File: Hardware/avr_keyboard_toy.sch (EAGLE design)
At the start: 20 parts, among them IC1 7805T, IC2 MCP23017SP, U1 ATMEGA328P-PU

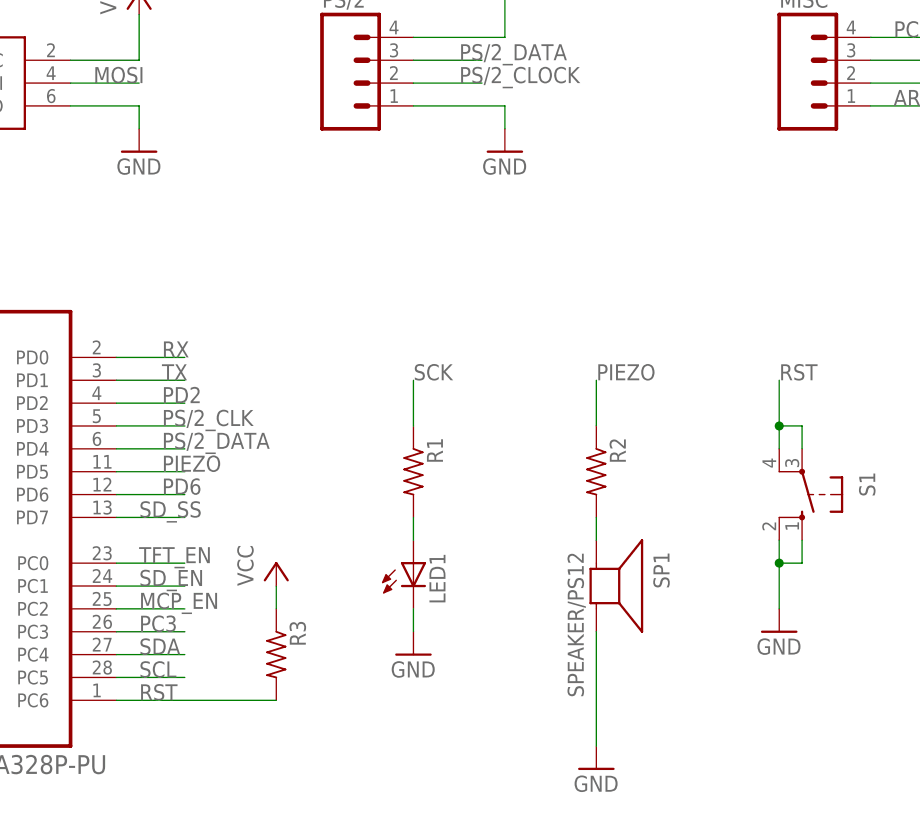
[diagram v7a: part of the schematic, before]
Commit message: Finished layout for rev. A board
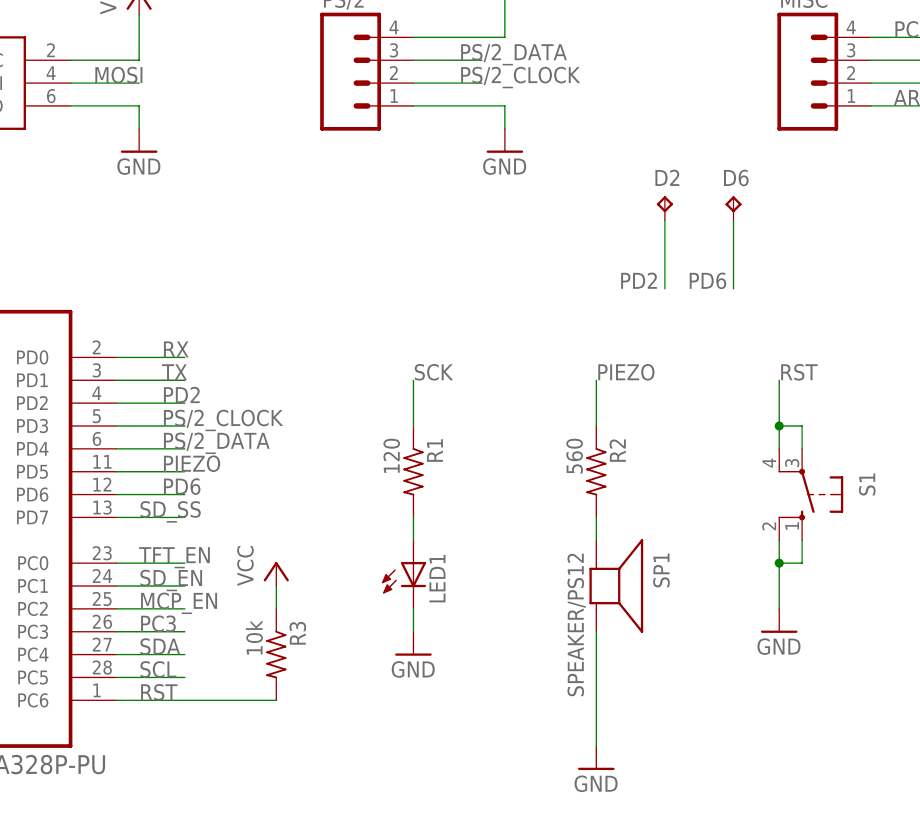
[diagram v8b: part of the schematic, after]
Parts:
- added D2, D6: TPB1,27, testpad:TPB1,27
- R1: value (none) -> 120
- R2: value (none) -> 560
- R3: value (none) -> 10k
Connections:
- removed net PS/2_CLK: U1.PD3
- net PD2: now also D2.TP
- net PD6: now also D6.TP
- net PS/2_CLOCK: now also U1.PD3
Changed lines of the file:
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@@
 <part name="ISP1" library="adafruit" deviceset="AVRISP" device="-6"/>
 <part name="LED1" library="adafruit" deviceset="LED" device="3MM"/>
-<part name="R1" library="adafruit" deviceset="R-US_" device="0204/5"/>
-<part name="R2" library="adafruit" deviceset="R-US_" device="0204/5"/>
-<part name="R3" library="adafruit" deviceset="R-US_" device="0204/5"/>
+<part name="R1" library="adafruit" deviceset="R-US_" device="0204/5" value="120"/>
+<part name="R2" library="adafruit" deviceset="R-US_" device="0204/5" value="560"/>
+<part name="R3" library="adafruit" deviceset="R-US_" device="0204/5" value="10k"/>
 <part name="SP1" library="adafruit" deviceset="SPEAKER" device="/PS12"/>
 <part name="S1" library="switch-omron" deviceset="10-XX" device=""/>
@@
 <part name="MISC" library="SparkFun-Connectors" deviceset="M04" device="PTH"/>
 <part name="GND4" library="supply1" deviceset="GND" device=""/>
+<part name="D2" library="testpad" deviceset="TP" device="B1,27"/>
+<part name="D6" library="testpad" deviceset="TP" device="B1,27"/>
 </parts>
 <sheets>
@@
 <instance part="MISC" gate="G$1" x="154.94" y="147.32"/>
 <instance part="GND4" gate="1" x="175.26" y="139.7"/>
+<instance part="D2" gate="G$1" x="137.16" y="134.62"/>
+<instance part="D6" gate="G$1" x="144.78" y="134.62"/>
 </instances>
 <busses>
@@
 </segment>
 </net>
-<net name="PS/2_CLK" class="0">
+<net name="PS/2_DATA" class="0">
+<segment>
+<pinref part="U1" gate="A" pin="PD4"/>
+<wire x1="83.82" y1="106.68" x2="76.2" y2="106.68" width="0.1524" layer="91"/>
+<label x="81.28" y="106.68" size="1.778" layer="95"/>
+</segment>
+<segment>
+<pinref part="PS/2" gate="G$1" pin="3"/>
+<wire x1="116.84" y1="149.86" x2="109.22" y2="149.86" width="0.1524" layer="91"/>
+<label x="114.3" y="149.86" size="1.778" layer="95"/>
+</segment>
+</net>
+<net name="PS/2_CLOCK" class="0">
+<segment>
+<pinref part="PS/2" gate="G$1" pin="2"/>
+<wire x1="116.84" y1="147.32" x2="109.22" y2="147.32" width="0.1524" layer="91"/>
+<label x="114.3" y="147.32" size="1.778" layer="95"/>
+</segment>
 <segment>
 <pinref part="U1" gate="A" pin="PD3"/>
@@
 </segment>
 </net>
-<net name="PS/2_DATA" class="0">
-<segment>
-<pinref part="U1" gate="A" pin="PD4"/>
-<wire x1="83.82" y1="106.68" x2="76.2" y2="106.68" width="0.1524" layer="91"/>
-<label x="81.28" y="106.68" size="1.778" layer="95"/>
-</segment>
-<segment>
-<pinref part="PS/2" gate="G$1" pin="3"/>
-<wire x1="116.84" y1="149.86" x2="109.22" y2="149.86" width="0.1524" layer="91"/>
-<label x="114.3" y="149.86" size="1.778" layer="95"/>
-</segment>
-</net>
-<net name="PS/2_CLOCK" class="0">
-<segment>
-<pinref part="PS/2" gate="G$1" pin="2"/>
-<wire x1="116.84" y1="147.32" x2="109.22" y2="147.32" width="0.1524" layer="91"/>
-<label x="114.3" y="147.32" size="1.778" layer="95"/>
-</segment>
-</net>
 <net name="N$3" class="0">
 <segment>
@@
 <label x="81.28" y="111.76" size="1.778" layer="95"/>
 </segment>
+<segment>
+<pinref part="D2" gate="G$1" pin="TP"/>
+<wire x1="137.16" y1="124.46" x2="137.16" y2="132.08" width="0.1524" layer="91"/>
+<label x="132.08" y="124.46" size="1.778" layer="95"/>
+</segment>
 </net>
 <net name="PD6" class="0">
@@
 <label x="81.28" y="101.6" size="1.778" layer="95"/>
 </segment>
-</net>
+<segment>
+<pinref part="D6" gate="G$1" pin="TP"/>
+<wire x1="144.78" y1="124.46" x2="144.78" y2="132.08" width="0.1524" layer="91"/>
+<label x="139.7" y="124.46" size="1.778" layer="95"/>
+</segment>
+</net>
